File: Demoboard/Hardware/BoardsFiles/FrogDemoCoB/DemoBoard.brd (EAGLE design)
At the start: 103.5 x 66.2 mm, 94 parts, among them IC1 LM20125MHE_NOPB, IC2 LM20125MHE_NOPB, J5 DM3AT-SF-PEJM5, J6 SAMTEC-MMS-105-02-X-SVJ, Q1 IRLML0030TRPBF, Q2 MMBT3904,215, Q3 MMBT3904,215, Q4 BC846B,235, Q5 BC846B,235, Q6 BC846B,235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

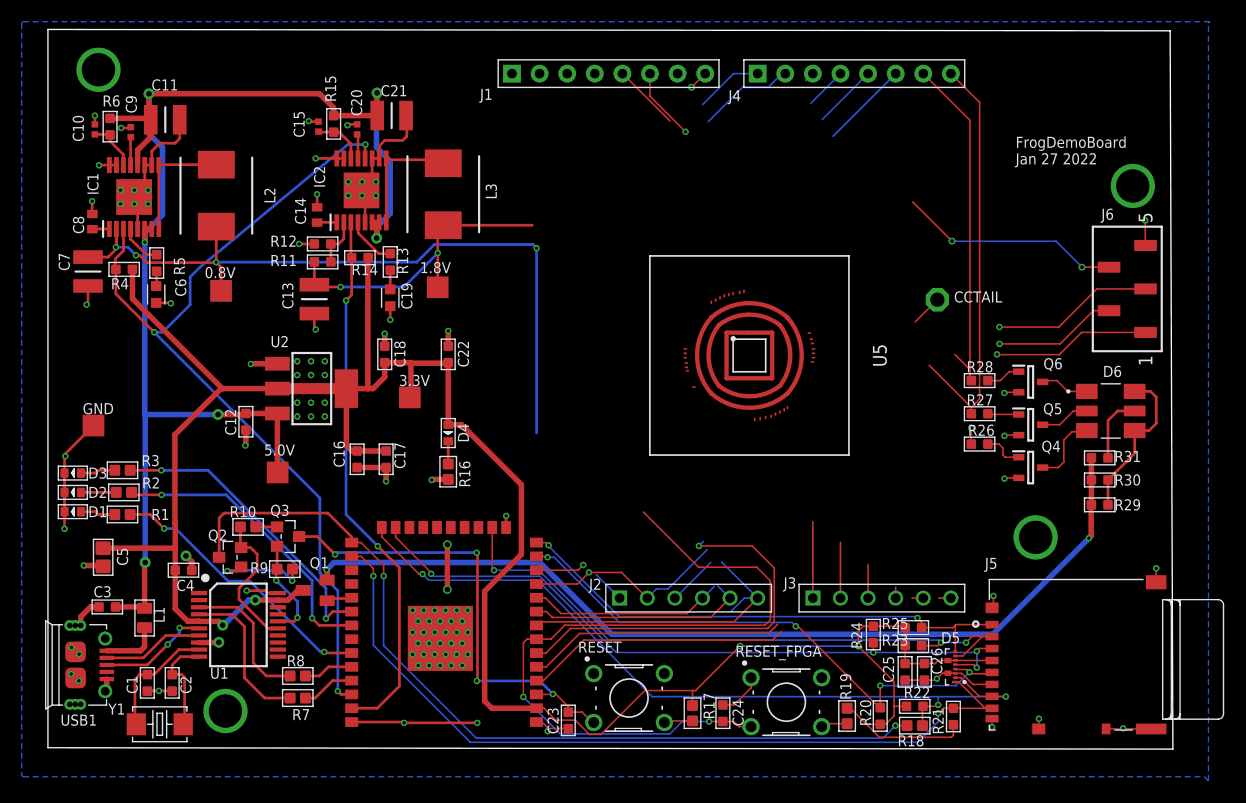
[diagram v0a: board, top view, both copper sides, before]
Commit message: Update ChipOnBoard and add assembly drawing
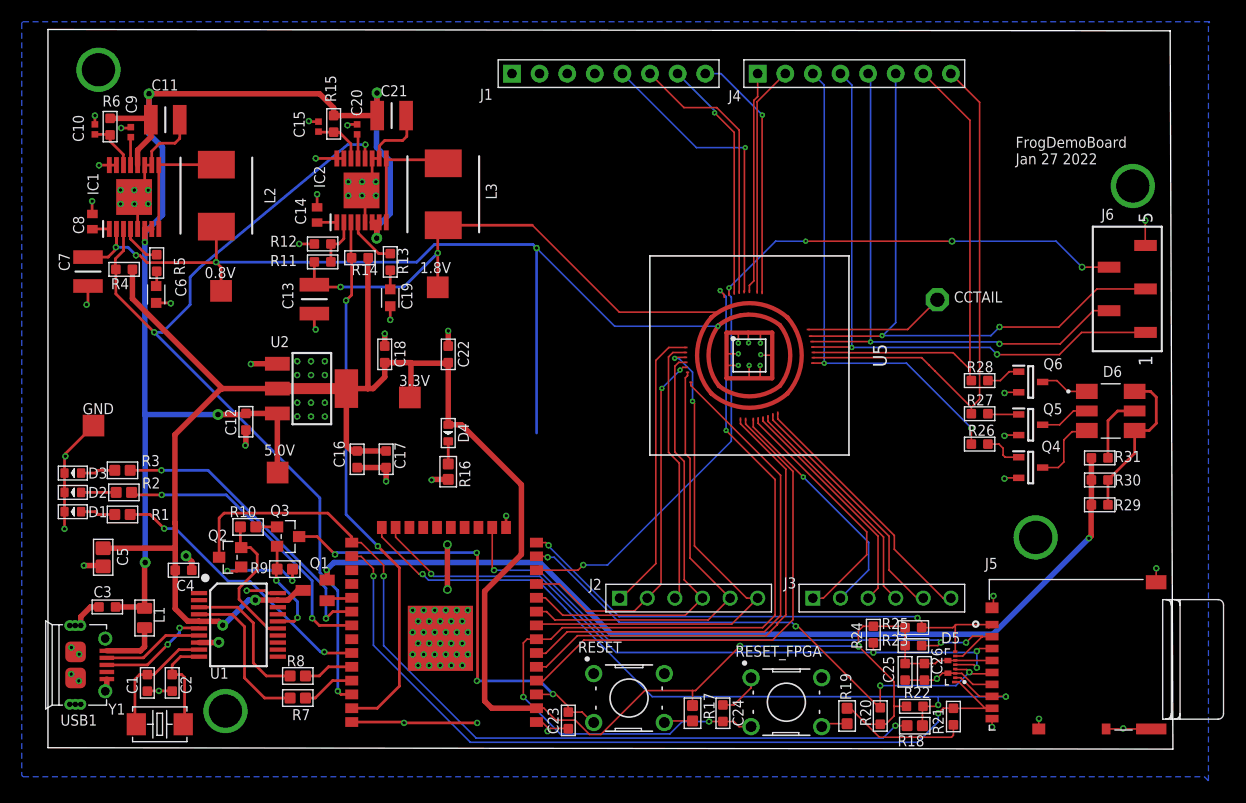
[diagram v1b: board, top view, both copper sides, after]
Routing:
- net CLK: track 25.8 -> 76.2 mm, vias 3 -> 5
- net GPIO18: track 2.40 -> 45.6 mm, vias 1 -> 2
- net GPIO21: track 18.4 -> 57.4 mm, vias 1 -> 2
- net GPIO22: track 17.3 -> 53.5 mm, vias 1 -> 2
- net GPIO23: track 23.0 -> 57.2 mm, vias 1 -> 2
- net GND: track 133.2 -> 158.5 mm, vias 103 -> 111
- net GPIO11: track 3.07 -> 26.7 mm
- net 1.8V: track 29.0 -> 52.5 mm
- net 0.8V: track 69.8 -> 92.8 mm, vias 4 -> 5
- net GPIO12: track 1.12 -> 24.0 mm
- net GPIO8: track 18.0 -> 40.2 mm
- net GPIO5: track 0.30 -> 22.3 mm, vias 0 -> 1
- net GPIO13: track 1.04 -> 22.9 mm
- net PROG_CLK: track 24.4 -> 46.2 mm
- net GPIO0: track 1.81 -> 23.2 mm
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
